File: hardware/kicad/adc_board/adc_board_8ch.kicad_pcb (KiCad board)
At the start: 2 copper layers, 88 x 66 mm, 10 parts, among them J1 ELECTRODES, J2 SPI_HOST, J3 PWR_CTRL, U1 ADS131M08

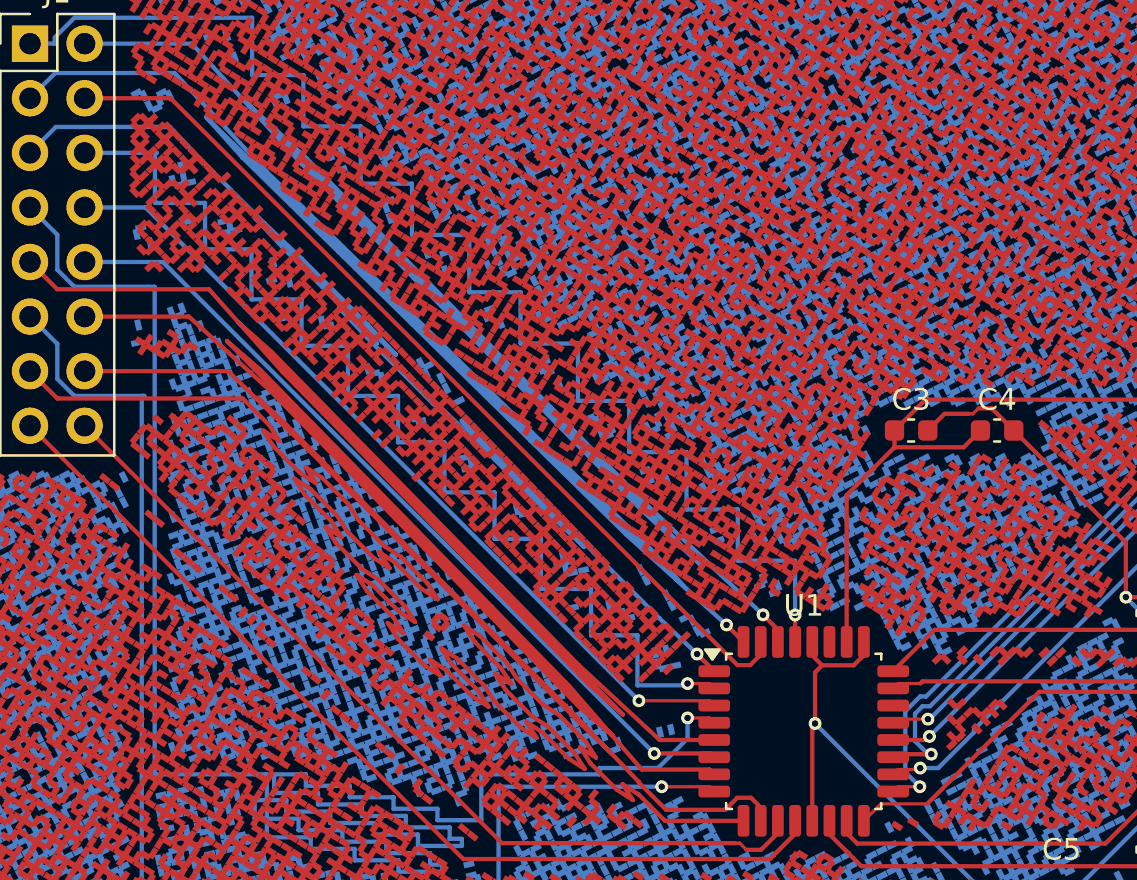
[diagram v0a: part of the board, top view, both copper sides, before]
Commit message: fix(kicad): restore AIN4P direct route
Co-authored-by: Copilot <223556219+Copilot@users.noreply.github.com>
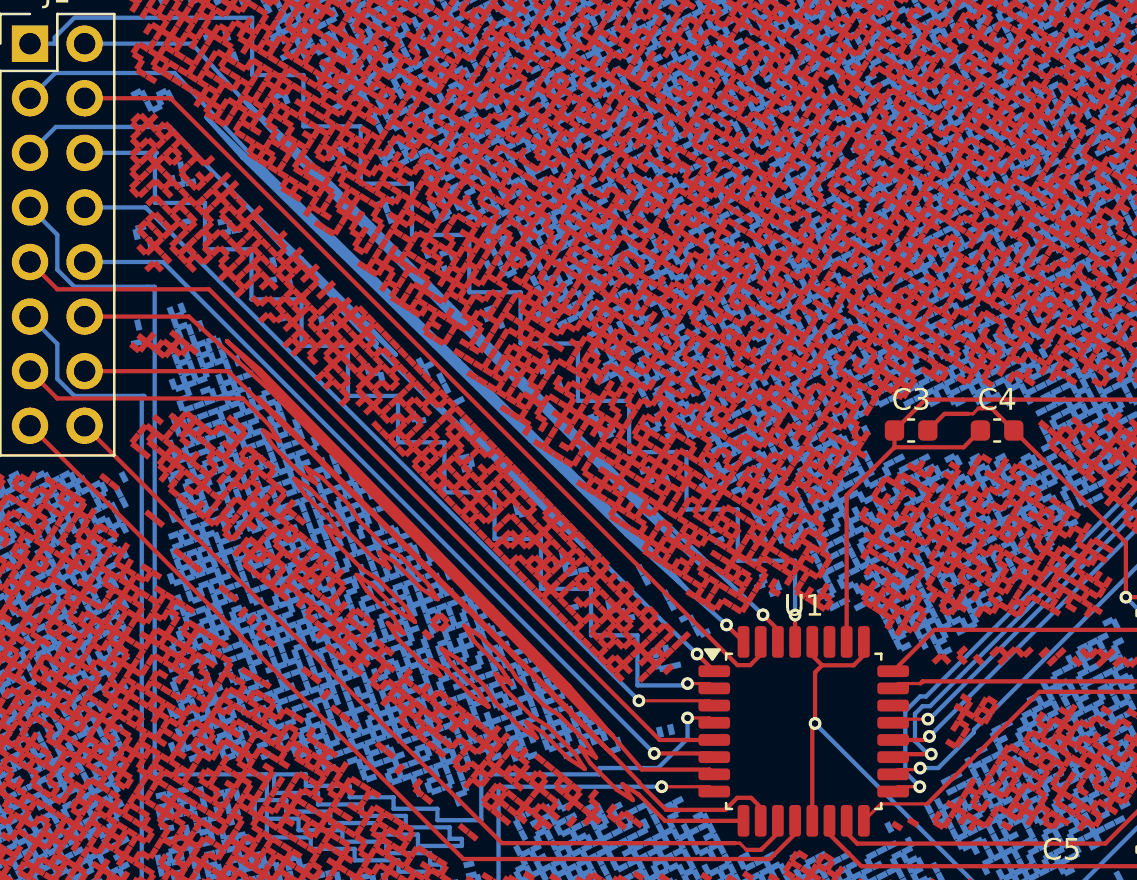
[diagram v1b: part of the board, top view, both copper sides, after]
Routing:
- net AIN4P: track 92.2 -> 41.0 mm
